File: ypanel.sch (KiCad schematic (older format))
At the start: 25 parts, among them IC2 TSL2561, J1 XF2M-1015-1A, J2 U.FL-R-SMT-1, J3 BATTERY CONNECTOR, J4 B2B-PH-SM4-TB_LF__SN_, U1 SWLP.12.B, U3 SW_SPDT, U4 SW_SPDT

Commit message: repaired schematic so it matches PCB
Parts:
- removed D11, D12: bypassdiode, solarpcb:SB-Diode, symbol ypanel_lib:bypassdiode
- removed D30: MSS1P4-M3_89A, solarpcb:MICROSMP, symbol ypanel-rescue:MSS1P4-M3_89A-symbols
- removed R10, R16: 0, Resistor_SMD:R_0402_1005Metric, symbol ypanel-rescue:0OHM-0603-1_10W-5%
- removed SC1, SC2, SC3, SC4, SC5, SC6: solarcell, custom-footprints:KXOB25-05X3F, symbol ypanel_lib:solarcell
- added C1: 1.0uF, Capacitor_SMD:C_0402_1005Metric, symbol SolarCellX_v3-rescue:1.0UF-0603-16V-10%-misc-circuits-cache-misc-circuits-rescue
- added C11, C6: 100uF, Capacitor_SMD:C_0603_1608Metric, symbol SolarCellX_v3-rescue:0.1UF-0603-25V-(+80_-20%)-misc-circuits-cache-misc-circuit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
- added C2, C9: 0.1uF, Capacitor_SMD:C_0402_1005Metric, symbol SolarCellX_v3-rescue:0.1UF-0603-25V-(+80_-20%)-misc-circuits-cache-misc-circuit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
- added C3, C8: 4.7uF, Capacitor_SMD:C_0402_1005Metric, symbol SolarCellX_v3-rescue:4.7UF0603-misc-circuits-cache-misc-circuits-rescue
- added C4: 10nF, Capacitor_SMD:C_0402_1005Metric, symbol SolarCellX_v3-rescue:10NF-0603-50V-10%-misc-circuits-cache-misc-circuits-rescue
- added C7: 22uF, Capacitor_SMD:C_0402_1005Metric, symbol SolarCellX_v3-rescue:22UF-0805-6.3V-20%-misc-circuits-cache-misc-circuits-rescue
- added D1: SDM20U40-7, misc-circuits:SOD523, symbol SolarCellX_v3-rescue:DIODE-SOD523-misc-circuits-cache-misc-circuits-rescue
- added D11, D12: SBDiode, SolarCellParts:SB Diode, symbol SolarCellX_v3-rescue:SBDiode-SolarCellParts
- added D2, D30: MSS1P4-M3_89A, misc-circuits:MICROSMP, symbol SolarCellX_v3-rescue:MSS1P4-M3_89A-symbols
- added L1: 22uH-LPS4018-223MR, misc-circuits:LPS4018, symbol SolarCellX_v3-rescue:COILCRAFT-LPS4018-misc-circuits-cache-misc-circuits-rescue
- added L2: 10uH-LPS4018-103MR, misc-circuits:LPS4018, symbol SolarCellX_v3-rescue:COILCRAFT-LPS4018-misc-circuits-cache-misc-circuits-rescue
- added R1, R10, R11, R12, R13, R14, R15, R16, R19, R9: 0, Resistor_SMD:R_0402_1005Metric, symbol SolarCellX_v3-rescue:0OHM-0603-1_10W-5%-misc-circuits-cache-misc-circuits-rescue
- added R18: 0, Resistor_SMD:R_0402_1005Metric, symbol ypanel-rescue:0OHM-0603-1_10W-5%
- added R2: 7.32M, Resistor_SMD:R_0402_1005Metric, symbol SolarCellX_v3-rescue:1MOHM-0603-1_4W-5%-misc-circuits-cache-misc-circuits-rescue
- added R3: 5.62M, Resistor_SMD:R_0402_1005Metric, symbol SolarCellX_v3-rescue:1MOHM-0603-1_4W-5%-misc-circuits-cache-misc-circuits-rescue
- added R4: 374K, Resistor_SMD:R_0402_1005Metric, symbol SolarCellX_v3-rescue:1MOHM-0603-1_4W-5%-misc-circuits-cache-misc-circuits-rescue
- added R5, R8: 8.25M, Resistor_SMD:R_0402_1005Metric, symbol SolarCellX_v3-rescue:1MOHM-0603-1_4W-5%-misc-circuits-cache-misc-circuits-rescue
- added R6: 4.53M, Resistor_SMD:R_0402_1005Metric, symbol SolarCellX_v3-rescue:1MOHM-0603-1_4W-5%-misc-circuits-cache-misc-circuits-rescue
- added R7: 4.75M, Resistor_SMD:R_0402_1005Metric, symbol SolarCellX_v3-rescue:1MOHM-0603-1_4W-5%-misc-circuits-cache-misc-circuits-rescue
- added SC1, SC2, SC3, SC4, SC5, SC6: SolarCell_Small, custom-footprints:KXOB25-05X3F, symbol SolarCellX_v3-rescue:SolarCell_Small-SolarCellParts
- added U2: Value, misc-circuits:QFN50P350X350X100-21N-D, symbol SolarCellX_v3-rescue:BQ25570RGRR-misc-circuits-cache-misc-circuits-rescue
- J4: symbol dk_Rectangular-Connectors-Headers-Male-Pins:B2B-PH-SM4-TB_LF__SN_ -> ypanel-rescue:B2B-PH-SM4-TB_LF__SN_-dk_Rectangular-Connectors-Headers-Male-Pins
- renumbered R1 to R1000, R9 to R17
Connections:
- net labels added: VBAT, VBAT_OK, VOUT_EN, VSOLAR_FULL
- net labels removed: pre-3V3
- wire segments 68 -> 170
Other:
- note added: "80% MPPT"
- note added: "BQ25570RGRR"
- note added: "COIL+"
- note added: "COIL-"
- note added: "Clockwise\n(while facing layer 1)"
- note added: "DNI"
- note added: "Energy Harvesting IC"
- note added: "External energy storage\nInput/Output"
- note added: "External\nPower Source\nInput\n(Solar)"
- note added: "Imin=280uA"
- note added: "MPPT Set Resistors"
- note added: "Sets of resistor dividers should = 13MOhm"
- note added: "VBAT_OK\nON: 3.51V\nOFF: 3.42V"
- note added: "VBAT_OV\n4.2V"
- note added: "VOUT=1.21V*((ROUT2+ROUT1)/ROUT1)"
- note added: "VOUT\n3.31"
- note added: "ZENER"
- note removed: "ignore"
- moved on the sheet: J3, R1000, R17, U3, U4

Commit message: Updated -Y
moved killswitches & flat-flex connector to new locations
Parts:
- C1: symbol SolarCellX_v3-rescue:1.0UF-0603-16V-10%-misc-circuits-cache-misc-circuits-rescue -> ypanel-rescue:1.0UF-0603-16V-10%-misc-circuits-cache-misc-circuits-rescue-SolarCellX_v3-rescue
- C11, C2, C6, C9: symbol SolarCellX_v3-rescue:0.1UF-0603-25V-(+80_-20%)-misc-circuits-cache-misc-circuits-rescue -> ypanel-rescue:0.1UF-0603-25V-(+80_-20%)-misc-circuits-cache-misc-circuits-rescue-SolarCellX_v3-rescue
- C3, C8: symbol SolarCellX_v3-rescue:4.7UF0603-misc-circuits-cache-misc-circuits-rescue -> ypanel-rescue:4.7UF0603-misc-circuits-cache-misc-circuits-rescue-SolarCellX_v3-rescue
- C4: symbol SolarCellX_v3-rescue:10NF-0603-50V-10%-misc-circuits-cache-misc-circuits-rescue -> ypanel-rescue:10NF-0603-50V-10%-misc-circuits-cache-misc-circuits-rescue-SolarCellX_v3-rescue
- C7: symbol SolarCellX_v3-rescue:22UF-0805-6.3V-20%-misc-circuits-cache-misc-circuits-rescue -> ypanel-rescue:22UF-0805-6.3V-20%-misc-circuits-cache-misc-circuits-rescue-SolarCellX_v3-rescue
- D1: symbol SolarCellX_v3-rescue:DIODE-SOD523-misc-circuits-cache-misc-circuits-rescue -> ypanel-rescue:DIODE-SOD523-misc-circuits-cache-misc-circuits-rescue-SolarCellX_v3-rescue
- D11, D12: symbol SolarCellX_v3-rescue:SBDiode-SolarCellParts -> ypanel-rescue:SBDiode-SolarCellParts-SolarCellX_v3-rescue
- D2, D30: symbol SolarCellX_v3-rescue:MSS1P4-M3_89A-symbols -> ypanel-rescue:MSS1P4-M3_89A-symbols-SolarCellX_v3-rescue
- L1, L2: symbol SolarCellX_v3-rescue:COILCRAFT-LPS4018-misc-circuits-cache-misc-circuits-rescue -> ypanel-rescue:COILCRAFT-LPS4018-misc-circuits-cache-misc-circuits-rescue-SolarCellX_v3-rescue
- R1, R10, R11, R12, R13, R14, R15, R16, R19, R9: symbol SolarCellX_v3-rescue:0OHM-0603-1_10W-5%-misc-circuits-cache-misc-circuits-rescue -> ypanel-rescue:0OHM-0603-1_10W-5%-misc-circuits-cache-misc-circuits-rescue-SolarCellX_v3-rescue
- R2, R3, R4, R5, R6, R7, R8: symbol SolarCellX_v3-rescue:1MOHM-0603-1_4W-5%-misc-circuits-cache-misc-circuits-rescue -> ypanel-rescue:1MOHM-0603-1_4W-5%-misc-circuits-cache-misc-circuits-rescue-SolarCellX_v3-rescue
- SC1, SC2, SC3, SC4, SC5, SC6: symbol SolarCellX_v3-rescue:SolarCell_Small-SolarCellParts -> ypanel-rescue:SolarCell_Small-SolarCellParts-SolarCellX_v3-rescue
- TP1, TP2, TP3: symbol Connector:TestPoint -> ypanel-rescue:TestPoint-Connector
- U2: symbol SolarCellX_v3-rescue:BQ25570RGRR-misc-circuits-cache-misc-circuits-rescue -> ypanel-rescue:BQ25570RGRR-misc-circuits-cache-misc-circuits-rescue-SolarCellX_v3-rescue

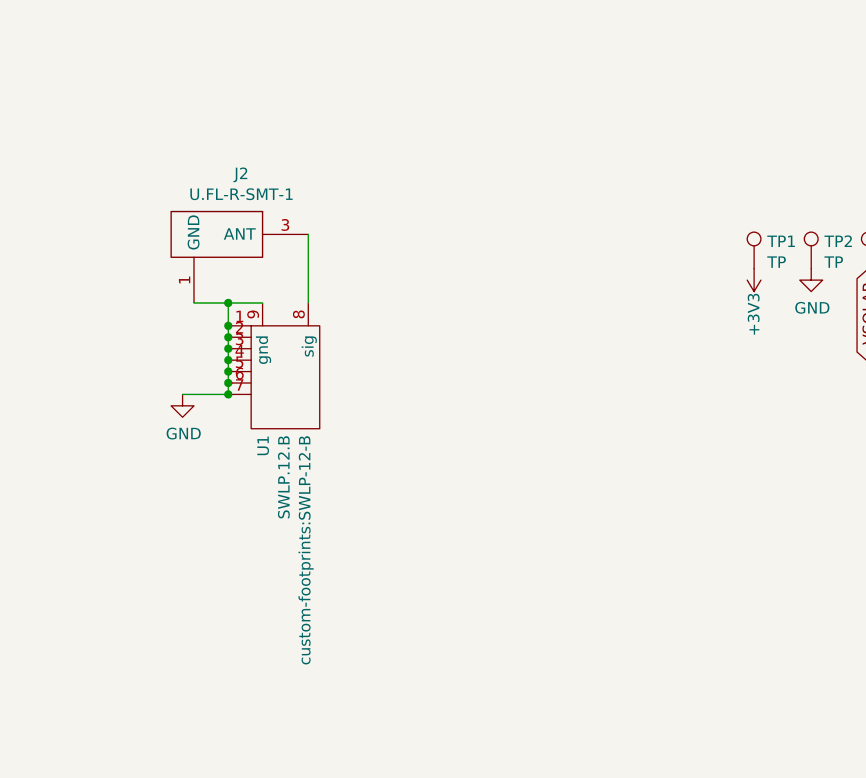
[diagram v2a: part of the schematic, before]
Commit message: Added new antenna to -Y
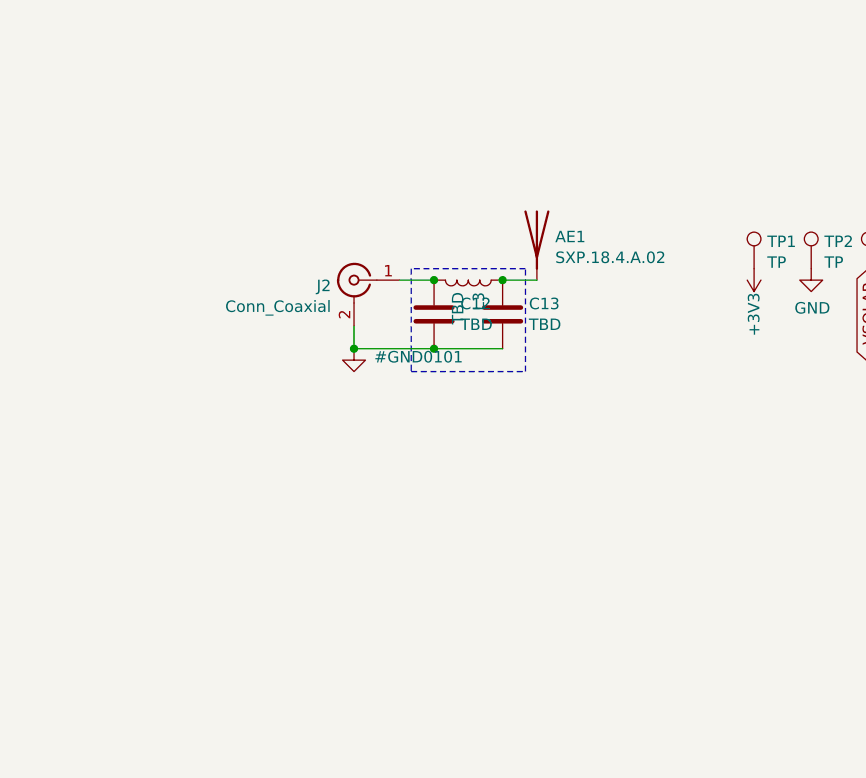
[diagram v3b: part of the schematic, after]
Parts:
- removed J2: U.FL-R-SMT-1, custom-footprints:U.FL-R-SMT-1, symbol ypanel-rescue:U.FL-R-SMT-1-symbols
- removed U1: SWLP.12.B, custom-footprints:SWLP-12-B, symbol ypanel_lib:SWLP.12.B
- added AE1: SXP.18.4.A.02, ypanel:SXP.18.4.A.02, symbol Device:Antenna
- added C12, C13: TBD, Capacitor_SMD:C_0201_0603Metric, symbol Device:C
- added J2: Conn_Coaxial, Connector_Coaxial:U.FL_Hirose_U.FL-R-SMT-1_Vertical, symbol Connector:Conn_Coaxial
- added L3: TBD, Inductor_SMD:L_0201_0603Metric, symbol Device:L
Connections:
- net GND: now also C12.2, C13.2, J2.2 (Ext)
- new net: AE1.1 (A), C13.1, L3.1
- new net: C12.1, J2.1 (In), L3.2
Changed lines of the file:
@@
 $EndDescr
-$Comp
-L ypanel_lib:SWLP.12.B U1
-U 1 1 5DB14A86
-P 7250 8900
-F 0 "U1" H 7528 8996 50  0000 L CNN
-F 1 "SWLP.12.B" H 7528 8905 50  0000 L CNN
-F 2 "custom-footprints:SWLP-12-B" H 7528 8814 50  0000 L CNN
-F 3 "" H 7250 8900 50  0001 C CNN
-	1    7250 8900
-	0    -1   1    0
-$EndComp
 $Comp
 L ypanel-rescue:XF2M-1015-1A-symbols-misc-circuits-rescue J1
@@
 Wire Wire Line
 	13050 3900 13600 3900
-$Comp
-L ypanel-rescue:U.FL-R-SMT-1-symbols J2
-U 1 1 5DC33039
-P 6950 8300
-F 0 "J2" H 6842 8565 50  0000 C CNN
-F 1 "U.FL-R-SMT-1" H 6842 8474 50  0000 C CNN
-F 2 "custom-footprints:U.FL-R-SMT-1" H 6650 8550 50  0001 L CNN
-F 3 "https://www.hirose.co.jp/cataloge_hp/ed_UFL_20141014.pdf" H 6650 8450 50  0001 L CNN
-F 4 "Hirose" H 6650 8150 50  0001 L CNN "Manufacturer_Name"
-F 5 "U.FL-R-SMT-1" H 6650 8050 50  0001 L CNN "Manufacturer_Part_Number"
-	1    6950 8300
-	-1   0    0    -1
-$EndComp
-Wire Wire Line
-	7350 8300 7350 8600
-Wire Wire Line
-	7150 8600 7000 8600
-Wire Wire Line
-	7000 9000 7000 8950
-Connection ~ 7000 8600
-Wire Wire Line
-	7000 8600 6850 8600
-Connection ~ 7000 8700
-Wire Wire Line
-	7000 8700 7000 8600
-Connection ~ 7000 8750
-Wire Wire Line
-	7000 8750 7000 8700
-Connection ~ 7000 8800
-Wire Wire Line
-	7000 8800 7000 8750
-Connection ~ 7000 8850
-Wire Wire Line
-	7000 8850 7000 8800
-Connection ~ 7000 8900
-Wire Wire Line
-	7000 8900 7000 8850
-Connection ~ 7000 8950
-Wire Wire Line
-	7000 8950 7000 8900
-$Comp
-L ypanel-rescue:GND-power #PWR0115
-U 1 1 5DC4B261
-P 6800 9000
-F 0 "#PWR0115" H 6800 8750 50  0001 C CNN
-F 1 "GND" H 6805 8827 50  0000 C CNN
-F 2 "" H 6800 9000 50  0001 C CNN
-F 3 "" H 6800 9000 50  0001 C CNN
-	1    6800 9000
-	1    0    0    -1
-$EndComp
-Wire Wire Line
-	6800 9000 7000 9000
-Connection ~ 7000 9000
 Wire Wire Line
 	12000 4000 12150 4000
@@
 Wire Wire Line
 	1840 8150 1850 8150
+$Comp
+L Device:Antenna AE1
+U 1 1 5E47036D
+P 8350 8300
+F 0 "AE1" H 8430 8289 50  0000 L CNN
+F 1 "SXP.18.4.A.02" H 8430 8198 50  0000 L CNN
+F 2 "ypanel:SXP.18.4.A.02" H 8350 8300 50  0001 C CNN
+F 3 "~" H 8350 8300 50  0001 C CNN
+	1    8350 8300
+	1    0    0    -1
+$EndComp
+$Comp
+L Device:L L3
+U 1 1 5E48B702
+P 8050 8500
+F 0 "L3" H 8102 8546 50  0000 L CNN
+F 1 "TBD" H 8102 8455 50  0000 L CNN
+F 2 "Inductor_SMD:L_0201_0603Metric" H 8050 8500 50  0001 C CNN
+F 3 "~" H 8050 8500 50  0001 C CNN
+	1    8050 8500
+	0    1    1    0
+$EndComp
+$Comp
+L Device:C C12
+U 1 1 5E48D592
+P 7900 8650
+F 0 "C12" H 8015 8696 50  0000 L CNN
+F 1 "TBD" H 8015 8605 50  0000 L CNN
+F 2 "Capacitor_SMD:C_0201_0603Metric" H 7938 8500 50  0001 C CNN
+F 3 "~" H 7900 8650 50  0001 C CNN
+	1    7900 8650
+	1    0    0    -1
+$EndComp
+$Comp
+L Device:C C13
+U 1 1 5E48F12E
+P 8200 8650
+F 0 "C13" H 8315 8696 50  0000 L CNN
+F 1 "TBD" H 8315 8605 50  0000 L CNN
+F 2 "Capacitor_SMD:C_0201_0603Metric" H 8238 8500 50  0001 C CNN
+F 3 "~" H 8200 8650 50  0001 C CNN
+	1    8200 8650
+	1    0    0    -1
+$EndComp
+$Comp
+L Connector:Conn_Coaxial J2
+U 1 1 5E49C20B
+P 7550 8500
+F 0 "J2" H 7650 8475 50  0000 L CNN
+F 1 "Conn_Coaxial" H 7650 8384 50  0000 L CNN
+F 2 "Connector_Coaxial:U.FL_Hirose_U.FL-R-SMT-1_Vertical" H 7550 8500 50  0001 C CNN
+F 3 " ~" H 7550 8500 50  0001 C CNN
+	1    7550 8500
+	-1   0    0    -1
+$EndComp
+Wire Wire Line
+	8200 8500 8350 8500
+Wire Wire Line
+	7750 8500 7900 8500
+Connection ~ 7900 8500
+Wire Wire Line
+	8200 8800 7900 8800
+$Comp
+L ypanel-rescue:GND-power #GND0101
+U 1 1 5E4E54D7
+P 7550 8800
+F 0 "#GND0101" H 7638 8763 50  0000 L CNN
+F 1 "GND-power" H 7555 8627 50  0001 C CNN
+F 2 "" H 7550 8800 50  0001 C CNN
+F 3 "" H 7550 8800 50  0001 C CNN
+	1    7550 8800
+	1    0    0    -1
+$EndComp
+Wire Wire Line
+	7550 8700 7550 8800
+Wire Wire Line
+	7900 8800 7550 8800
+Connection ~ 7900 8800
+Connection ~ 7550 8800
+Wire Notes Line
+	7800 8450 7800 8900
+Wire Notes Line
+	7800 8900 8300 8900
+Wire Notes Line
+	8300 8900 8300 8450
+Wire Notes Line
+	8300 8450 7800 8450
+Connection ~ 8200 8500
 $EndSCHEMATC

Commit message: fixed antenna footprint and regenerated step file
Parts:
- AE1: footprint ypanel:SXP.18.4.A.02 -> spacecraft-footprints:SXP.18.4.A.02
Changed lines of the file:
@@
 EESchema Schematic File Version 4
 LIBS:ypanel-cache
-EELAYER 30 0
+EELAYER 26 0
 EELAYER END
 $Descr A3 16535 11693
@@
 F 0 "AE1" H 8430 8289 50  0000 L CNN
 F 1 "SXP.18.4.A.02" H 8430 8198 50  0000 L CNN
-F 2 "ypanel:SXP.18.4.A.02" H 8350 8300 50  0001 C CNN
+F 2 "spacecraft-footprints:SXP.18.4.A.02" H 8350 8300 50  0001 C CNN
 F 3 "~" H 8350 8300 50  0001 C CNN
 	1    8350 8300

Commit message: clean up & manufacturing output for v3
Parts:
- removed C12, C13: TBD, Capacitor_SMD:C_0201_0603Metric, symbol Device:C
- removed L3: TBD, Inductor_SMD:L_0201_0603Metric, symbol Device:L
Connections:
- net at AE1.1 (A): now also J2.1 (In)
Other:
- moved on the sheet: AE1
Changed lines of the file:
@@
 EESchema Schematic File Version 4
-LIBS:ypanel-cache
-EELAYER 26 0
+EELAYER 30 0
 EELAYER END
 $Descr A3 16535 11693
@@
 	1840 8150 1850 8150
 $Comp
-L Device:Antenna AE1
-U 1 1 5E47036D
-P 8350 8300
-F 0 "AE1" H 8430 8289 50  0000 L CNN
-F 1 "SXP.18.4.A.02" H 8430 8198 50  0000 L CNN
-F 2 "spacecraft-footprints:SXP.18.4.A.02" H 8350 8300 50  0001 C CNN
-F 3 "~" H 8350 8300 50  0001 C CNN
-	1    8350 8300
-	1    0    0    -1
-$EndComp
-$Comp
-L Device:L L3
-U 1 1 5E48B702
-P 8050 8500
-F 0 "L3" H 8102 8546 50  0000 L CNN
-F 1 "TBD" H 8102 8455 50  0000 L CNN
-F 2 "Inductor_SMD:L_0201_0603Metric" H 8050 8500 50  0001 C CNN
-F 3 "~" H 8050 8500 50  0001 C CNN
-	1    8050 8500
-	0    1    1    0
-$EndComp
-$Comp
-L Device:C C12
-U 1 1 5E48D592
-P 7900 8650
-F 0 "C12" H 8015 8696 50  0000 L CNN
-F 1 "TBD" H 8015 8605 50  0000 L CNN
-F 2 "Capacitor_SMD:C_0201_0603Metric" H 7938 8500 50  0001 C CNN
-F 3 "~" H 7900 8650 50  0001 C CNN
-	1    7900 8650
-	1    0    0    -1
-$EndComp
-$Comp
-L Device:C C13
-U 1 1 5E48F12E
-P 8200 8650
-F 0 "C13" H 8315 8696 50  0000 L CNN
-F 1 "TBD" H 8315 8605 50  0000 L CNN
-F 2 "Capacitor_SMD:C_0201_0603Metric" H 8238 8500 50  0001 C CNN
-F 3 "~" H 8200 8650 50  0001 C CNN
-	1    8200 8650
-	1    0    0    -1
-$EndComp
-$Comp
 L Connector:Conn_Coaxial J2
 U 1 1 5E49C20B
@@
 	-1   0    0    -1
 $EndComp
-Wire Wire Line
-	8200 8500 8350 8500
-Wire Wire Line
-	7750 8500 7900 8500
-Connection ~ 7900 8500
-Wire Wire Line
-	8200 8800 7900 8800
 $Comp
 L ypanel-rescue:GND-power #GND0101
@@
 	7550 8700 7550 8800
 Wire Wire Line
-	7900 8800 7550 8800
-Connection ~ 7900 8800
-Connection ~ 7550 8800
-Wire Notes Line
-	7800 8450 7800 8900
-Wire Notes Line
-	7800 8900 8300 8900
-Wire Notes Line
-	8300 8900 8300 8450
-Wire Notes Line
-	8300 8450 7800 8450
-Connection ~ 8200 8500
+	7750 8500 7900 8500
+$Comp
+L Device:Antenna AE1
+U 1 1 5E47036D
+P 7900 8300
+F 0 "AE1" H 7980 8289 50  0000 L CNN
+F 1 "SXP.18.4.A.02" H 7980 8198 50  0000 L CNN
+F 2 "spacecraft-footprints:SXP.18.4.A.02" H 7900 8300 50  0001 C CNN
+F 3 "~" H 7900 8300 50  0001 C CNN
+	1    7900 8300
+	1    0    0    -1
+$EndComp
 $EndSCHEMATC
